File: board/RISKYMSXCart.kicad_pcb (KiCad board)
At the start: 4 copper layers, 71.9 x 55.5 mm, 38 parts, among them CN1 MSX_CART, IC8 LM1117MPX-3.3, J1 Conn_01x02, J2 Conn_01x02, J7 USB_1, J8 Conn_01x02, U1 CH32V307VCT6, U2 MCP6001-OT

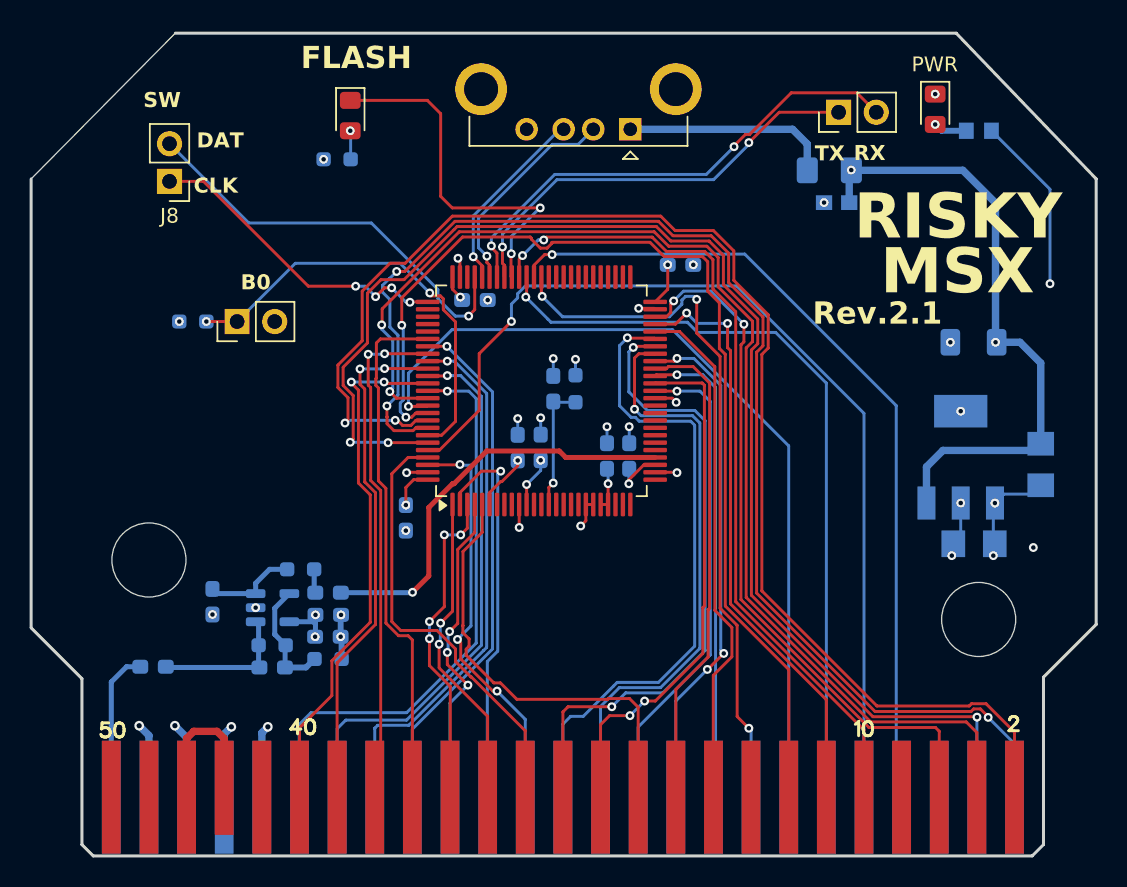
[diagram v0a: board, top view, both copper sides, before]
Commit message: Nextor and some Terminal improvements (#26)
* Add Nextor support for USB mass-storage in firmware

- Introduced Nextor mapper in cart.h and implemented its handler in nextor.c.
- Added functions for Nextor command processing, including Read, Write, and Status commands.
- Implemented raw disk interface in raw_disk.c to handle USB stick operations directly.
- Updated main.c to include Nextor service calls based on the cartridge type.
- Defined mailbox communication protocol for Nextor in nextor.h.
- Added necessary structures and constants for managing disk geometry and state.
- Ensured IRQ safety for mailbox operations and command handling.

* Add Nextor ROM flashing support and update menu options

* Update Makefile and programflash.c for improved flashing process and progress reporting

* Refactor base increment calculation in internal_refresh for improved precision and clarity

* Add Nextor

* Initial SCC on Nextor

* Update firmware version to v4.0.1, add CART.NXT, and modify Makefile for Nextor support

* New PCB v2.2

* Update active layer and visible layers in RISKYMSXCart.kicad_prl configuration

* Refactor SCC memory management to use a static instance and update optimization level in utils.c

* Implement alphabetical file caching and invalidate cache on USB remount

* Refactor alphabetical file caching to use page boundaries for improved memory management and update README with new file listing behavior

* Add automatic mapper detection for ROM flashing and update version to v4.1.0
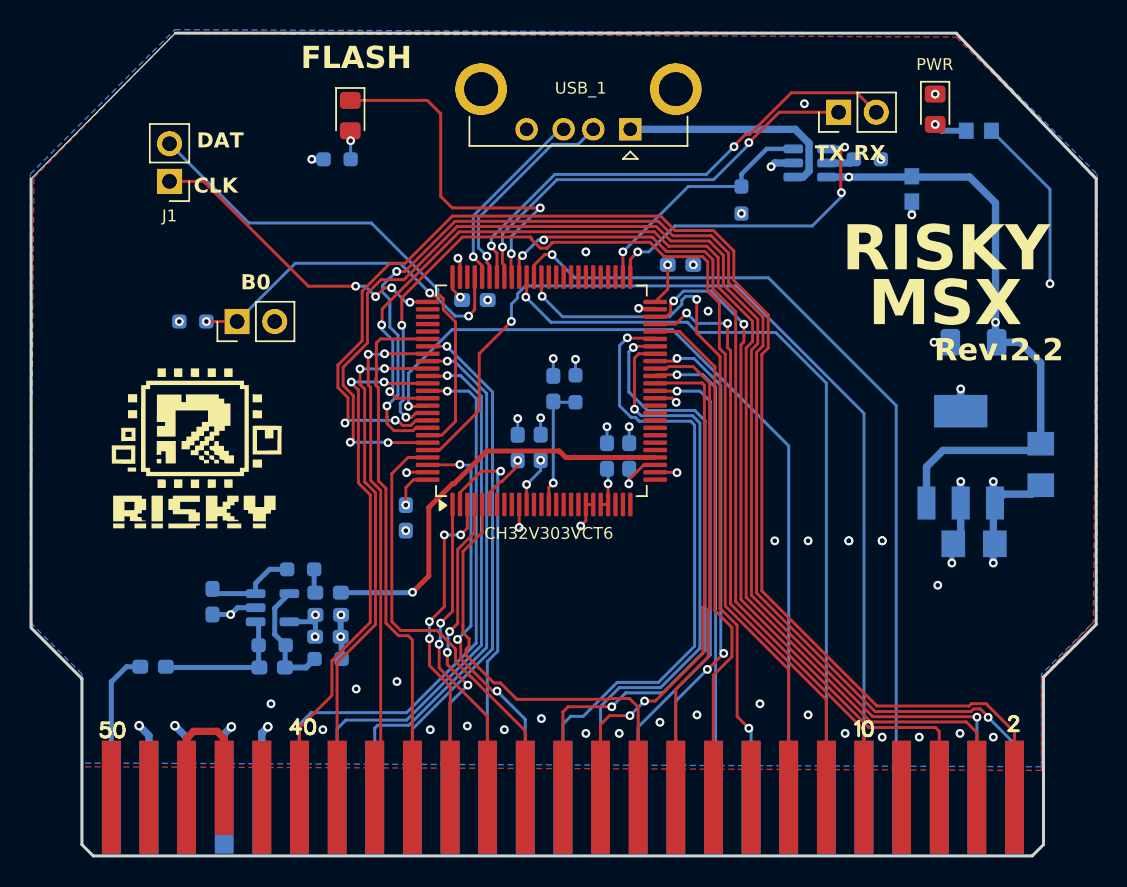
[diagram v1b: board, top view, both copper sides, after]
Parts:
- removed @HOLE1 (x2): , 
- removed F2: 0.5A, Fuse:Fuse_1206_3216Metric_Pad1.42x1.75mm_HandSolder
- added G***: LOGO, footprints:RIKSYLOGOMINI, F.Cu at (123.8, 105.2)
- added R1: 150k, Resistor_SMD:R_0603_1608Metric_Pad0.98x0.95mm_HandSolder, B.Cu at (169.0, 85.8)
- added R3: 10k, Resistor_SMD:R_0603_1608Metric_Pad0.98x0.95mm_HandSolder, B.Cu at (160.5, 88.5)
- added U1: CH217K, Package_TO_SOT_SMD:SOT-23-6, B.Cu at (165.1, 86.0)
- C1: renamed from C7; value 100nF -> 100n
- C10: renamed from C1; value 100nF -> 100n
- C11: renamed from C3; value 10uF -> 10u
- C12: renamed from C20; value 4.7uF -> 4.7u
- C13: renamed from C14; value 1nF -> 1n
- C14: renamed from C18; value 1uF -> 1u
- C15: renamed from C17; value 1nF -> 1n
- C16: renamed from C13; value 1uF -> 1u
- C17: renamed from C19; value 100nF -> 100n
- C18: renamed from C12; value 4.7uF -> 4.7u
- C2: renamed from C10; value 100nF -> 100n
- C3: renamed from C9; value 100nF -> 100n
- C4: renamed from C11; value 100nF -> 100n
- C5: renamed from C2; value 100nF -> 100n
- C6: renamed from C4; value 100nF -> 100n
- C7: renamed from C5; value 100nF -> 100n
- C8: renamed from C6; value 100nF -> 100n
- C9: renamed from C8; value 100nF -> 100n
- U2: renamed from U1; value CH32V307VCT6 -> CH32V303VCT6
- moved C11 5.16 mm to (172.0, 87.8), turned to -90 degrees
- renumbered D5 to D2, IC8 to IC1, J8 to J1, J1 to J3, J7 to J4, R4 to R2, R1 to R4, R10 to R6, R9 to R7, R2 to R8, R3 to R9, U2 to U3
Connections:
- U2 pad 51: unconnected-(U1-PB12(FT)-Pad51) -> /VBUS
- U2 pad 52: unconnected-(U1-PB13(FT)-Pad52) -> /FLAG
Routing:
- net /VBUS: track 0.00 -> 21.9 mm, vias 0 -> 3
- net /FLAG: track 0.00 -> 16.6 mm, vias 0 -> 1
- net +3.3V: track 38.0 -> 48.6 mm
- net GND: track 36.3 -> 46.3 mm, vias 27 -> 56
- net Net-(U1-ISET): track 0.00 -> 1.92 mm
- net Net-(J4-VBUS): track 14.1 -> 15.6 mm
- net +5V: track 56.0 -> 55.1 mm
- net (no net): vias 0 -> 1
- added copper zone on B.Cu, net GND
- added copper zone on F.Cu, net GND
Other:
- board text added: "Rev.2.2"
- board text removed: "Rev.2.1"
- board text removed: "SW"
